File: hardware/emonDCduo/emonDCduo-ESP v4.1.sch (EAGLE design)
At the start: 119 parts, among them IC1 ACS750LCA-050, IC2 ACS750LCA-050, Y1 32Khz

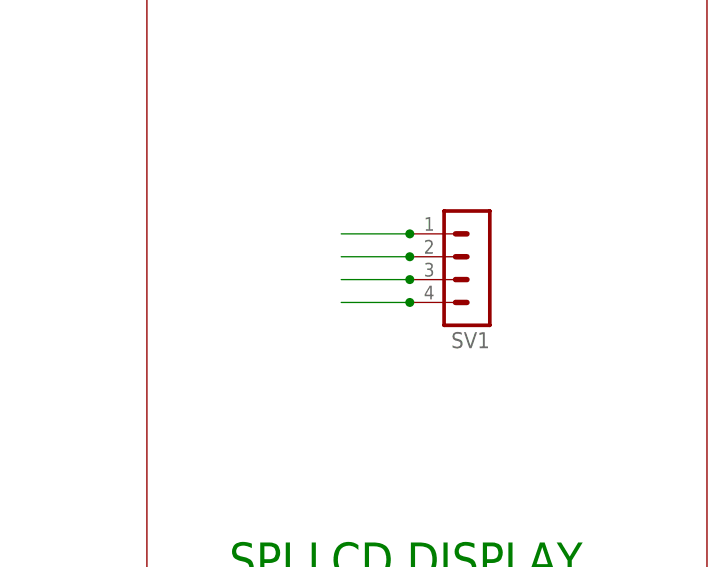
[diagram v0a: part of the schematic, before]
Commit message: commit v4.1
HV isolation improvements
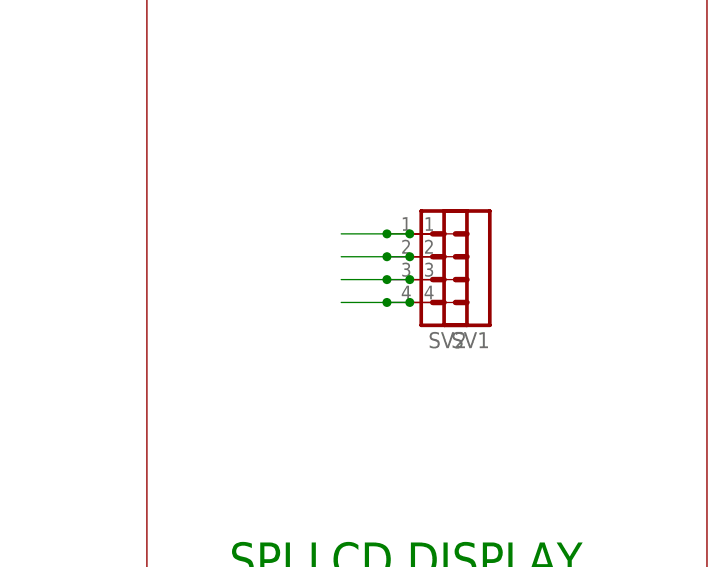
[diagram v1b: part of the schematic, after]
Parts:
- added SV2: (no value), con-lstb:MA04-1
- SJ1, SJ14, SJ3, SJ7: device jumper:SJ -> jumper:SJW
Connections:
- net +3V3: now also SV2.3
- net GND: now also SV2.4
- net SCL: now also SV2.2
- net SDA: now also SV2.1
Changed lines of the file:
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@@
 <?xml version="1.0" encoding="utf-8"?>
 <!DOCTYPE eagle SYSTEM "eagle.dtd">
-<eagle version="9.3.2">
+<eagle version="9.4.0">
 <drawing>
 <settings>
@@
 <clearance class="3" value="0.254"/>
 </class>
+<class number="4" name="HV" width="0" drill="0">
+<clearance class="4" value="0.508"/>
+</class>
 </classes>
 <parts>
@@
 <part name="TP11" library="testpad" library_urn="urn:adsk.eagle:library:385" deviceset="TP" device="PAD1-13Y" package3d_urn="urn:adsk.eagle:package:27947/1"/>
 <part name="D7" library="smf_10" deviceset="SMF*A" device="" technology="6.0"/>
-<part name="SJ3" library="jumper" library_urn="urn:adsk.eagle:library:252" deviceset="SJ" device="" package3d_urn="urn:adsk.eagle:package:15471/1"/>
-<part name="SJ7" library="jumper" library_urn="urn:adsk.eagle:library:252" deviceset="SJ" device="" package3d_urn="urn:adsk.eagle:package:15471/1"/>
+<part name="SJ3" library="jumper" library_urn="urn:adsk.eagle:library:252" deviceset="SJ" device="W" package3d_urn="urn:adsk.eagle:package:15507/1"/>
+<part name="SJ7" library="jumper" library_urn="urn:adsk.eagle:library:252" deviceset="SJ" device="W" package3d_urn="urn:adsk.eagle:package:15507/1"/>
 <part name="SJ8" library="microbuilder" deviceset="SOLDERJUMPER" device="CLOSED"/>
 <part name="SJ9" library="microbuilder" deviceset="SOLDERJUMPER" device="CLOSED"/>
@@
 <attribute name="OC_NEWARK" value=""/>
 </part>
-<part name="SV1" library="con-lstb" library_urn="urn:adsk.eagle:library:162" deviceset="MA04-1" device="" package3d_urn="urn:adsk.eagle:package:8337/1">
+<part name="SV1" library="con-lstb" deviceset="MA04-1" device="" package3d_urn="urn:adsk.eagle:package:8337/1">
 <attribute name="MF" value="MULTICOMP"/>
 <attribute name="MPN" value="2212S-04SG-85"/>
@@
 <part name="U$18" library="testpad_db" deviceset="TP" device="0.8MM"/>
 <part name="U$19" library="testpad_db" deviceset="TP" device="0.8MM"/>
-<part name="SJ1" library="jumper" library_urn="urn:adsk.eagle:library:252" deviceset="SJ" device="" package3d_urn="urn:adsk.eagle:package:15471/1"/>
-<part name="SJ14" library="jumper" library_urn="urn:adsk.eagle:library:252" deviceset="SJ" device="" package3d_urn="urn:adsk.eagle:package:15471/1"/>
+<part name="SJ1" library="jumper" library_urn="urn:adsk.eagle:library:252" deviceset="SJ" device="W" package3d_urn="urn:adsk.eagle:package:15507/1"/>
+<part name="SJ14" library="jumper" library_urn="urn:adsk.eagle:library:252" deviceset="SJ" device="W" package3d_urn="urn:adsk.eagle:package:15507/1"/>
+<part name="SV2" library="con-lstb" deviceset="MA04-1" device="" package3d_urn="urn:adsk.eagle:package:8337/1">
+<attribute name="MF" value="MULTICOMP"/>
+<attribute name="MPN" value="2212S-04SG-85"/>
+<attribute name="OC_FARNELL" value="1593460"/>
+</part>
 </parts>
 <sheets>
@@
 <attribute name="VALUE" x="-97.79" y="363.22" size="1.778" layer="96" rot="R90"/>
 </instance>
+<instance part="SV2" gate="1" x="256.54" y="452.12" smashed="yes" rot="R180">
+<attribute name="VALUE" x="257.81" y="462.28" size="1.778" layer="96" rot="R180"/>
+<attribute name="NAME" x="257.81" y="446.278" size="1.778" layer="95" rot="R180"/>
+</instance>
 </instances>
 <busses>
@@
 <segment>
 <pinref part="SV1" gate="1" pin="4"/>
-<wire x1="251.46" y1="449.58" x2="243.84" y2="449.58" width="0.1524" layer="91"/>
+<wire x1="251.46" y1="449.58" x2="248.92" y2="449.58" width="0.1524" layer="91"/>
 <junction x="251.46" y="449.58"/>
+<pinref part="SV2" gate="1" pin="4"/>
+<wire x1="248.92" y1="449.58" x2="243.84" y2="449.58" width="0.1524" layer="91"/>
+<junction x="248.92" y="449.58"/>
 </segment>
 <segment>
@@
 <segment>
 <pinref part="SV1" gate="1" pin="3"/>
-<wire x1="251.46" y1="452.12" x2="243.84" y2="452.12" width="0.1524" layer="91"/>
+<wire x1="251.46" y1="452.12" x2="248.92" y2="452.12" width="0.1524" layer="91"/>
 <junction x="251.46" y="452.12"/>
+<pinref part="SV2" gate="1" pin="3"/>
+<wire x1="248.92" y1="452.12" x2="243.84" y2="452.12" width="0.1524" layer="91"/>
+<junction x="248.92" y="452.12"/>
 </segment>
 <segment>
@@
 </segment>
 </net>
-<net name="LOAD-NEG-A" class="1">
+<net name="LOAD-NEG-A" class="4">
 <segment>
 <label x="-111.379" y="462.28" size="1.778" layer="95" rot="R180"/>
@@
 </segment>
 </net>
-<net name="SOURCE-POS-B" class="1">
+<net name="SOURCE-POS-B" class="4">
 <segment>
 <pinref part="MH3" gate="G$1" pin="MOUNT"/>
@@
 </segment>
 </net>
-<net name="LOAD-NEG-B" class="1">
+<net name="LOAD-NEG-B" class="4">
 <segment>
 <label x="-111.125" y="354.076" size="1.778" layer="95" rot="R180"/>
@@
 </segment>
 </net>
-<net name="SOURCE-POS-A" class="1">
+<net name="SOURCE-POS-A" class="4">
 <segment>
 <wire x1="-104.14" y1="434.34" x2="-106.68" y2="434.34" width="0.1524" layer="91"/>
@@
 <segment>
 <pinref part="SV1" gate="1" pin="1"/>
-<wire x1="251.46" y1="457.2" x2="243.84" y2="457.2" width="0.1524" layer="91"/>
+<wire x1="251.46" y1="457.2" x2="248.92" y2="457.2" width="0.1524" layer="91"/>
 <junction x="251.46" y="457.2"/>
+<pinref part="SV2" gate="1" pin="1"/>
+<wire x1="248.92" y1="457.2" x2="243.84" y2="457.2" width="0.1524" layer="91"/>
+<junction x="248.92" y="457.2"/>
 </segment>
 <segment>
@@
 <segment>
 <pinref part="SV1" gate="1" pin="2"/>
-<wire x1="251.46" y1="454.66" x2="243.84" y2="454.66" width="0.1524" layer="91"/>
+<wire x1="251.46" y1="454.66" x2="248.92" y2="454.66" width="0.1524" layer="91"/>
 <junction x="251.46" y="454.66"/>
+<pinref part="SV2" gate="1" pin="2"/>
+<wire x1="248.92" y1="454.66" x2="243.84" y2="454.66" width="0.1524" layer="91"/>
+<junction x="248.92" y="454.66"/>
 </segment>
 <segment>
@@
 </segment>
 </net>
-<net name="V_IN_POSTFUSE" class="1">
+<net name="V_IN_POSTFUSE" class="4">
 <segment>
 <wire x1="-111.76" y1="259.08" x2="-109.22" y2="259.08" width="0.1524" layer="91"/>
@@
 </segment>
 </net>
-<net name="V_IN_PREFUSE" class="1">
+<net name="V_IN_PREFUSE" class="4">
 <segment>
 <pinref part="F1" gate="G$1" pin="1"/>

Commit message: commit
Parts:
- SV1, SV2: device con-lstb:MA04-1 -> con-lstb-db:MA04-1
- renumbered REG1 to REG1_5V, REG2 to REG2_3.3
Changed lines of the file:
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@@
 <?xml version="1.0" encoding="utf-8"?>
 <!DOCTYPE eagle SYSTEM "eagle.dtd">
-<eagle version="9.4.0">
+<eagle version="9.3.2">
 <drawing>
 <settings>
@@
 </class>
 <class number="4" name="HV" width="0" drill="0">
-<clearance class="4" value="0.508"/>
+<clearance class="4" value="0.762"/>
 </class>
 </classes>
@@
 <part name="GND2" library="supply1" library_urn="urn:adsk.eagle:library:371" deviceset="GND" device=""/>
 <part name="GND23" library="supply1" library_urn="urn:adsk.eagle:library:371" deviceset="0V" device="" value="GND"/>
-<part name="REG2" library="burr-brown-db" deviceset="REG1117" device="" package3d_urn="urn:adsk.eagle:package:4940/1" value="REG1117-3.3V">
+<part name="REG2_3.3" library="burr-brown-db" deviceset="REG1117" device="" package3d_urn="urn:adsk.eagle:package:4940/1" value="REG1117-3.3V">
 <attribute name="MF" value="TEXAS INSTRUMENTS"/>
 <attribute name="MPN" value="REG1117-3.3"/>
@@
 <part name="J5" library="SparkFun-Connectors" deviceset="CONN_02" device=""/>
 <part name="MICRO_SD" library="MOLEX 47219-2001" deviceset="47219-2001_MICROSD" device=""/>
-<part name="REG1" library="burr-brown-db" deviceset="REG1117" device="" package3d_urn="urn:adsk.eagle:package:4940/1" value="REG1117-5.0V">
+<part name="REG1_5V" library="burr-brown-db" deviceset="REG1117" device="" package3d_urn="urn:adsk.eagle:package:4940/1" value="REG1117-5.0V">
 <attribute name="MF" value="TEXAS INSTRUMENTS"/>
 <attribute name="MPN" value="REG1117-5.0"/>
@@
 <attribute name="OC_NEWARK" value=""/>
 </part>
-<part name="SV1" library="con-lstb" deviceset="MA04-1" device="" package3d_urn="urn:adsk.eagle:package:8337/1">
+<part name="SV1" library="con-lstb-db" deviceset="MA04-1" device="">
 <attribute name="MF" value="MULTICOMP"/>
 <attribute name="MPN" value="2212S-04SG-85"/>
@@
 <part name="SJ1" library="jumper" library_urn="urn:adsk.eagle:library:252" deviceset="SJ" device="W" package3d_urn="urn:adsk.eagle:package:15507/1"/>
 <part name="SJ14" library="jumper" library_urn="urn:adsk.eagle:library:252" deviceset="SJ" device="W" package3d_urn="urn:adsk.eagle:package:15507/1"/>
-<part name="SV2" library="con-lstb" deviceset="MA04-1" device="" package3d_urn="urn:adsk.eagle:package:8337/1">
+<part name="SV2" library="con-lstb-db" deviceset="MA04-1" device="">
 <attribute name="MF" value="MULTICOMP"/>
 <attribute name="MPN" value="2212S-04SG-85"/>
@@
 <attribute name="VALUE" x="145.415" y="220.98" size="1.778" layer="96"/>
 </instance>
-<instance part="REG2" gate="G$1" x="114.3" y="243.84" smashed="yes">
+<instance part="REG2_3.3" gate="G$1" x="114.3" y="243.84" smashed="yes">
 <attribute name="NAME" x="106.68" y="249.555" size="1.778" layer="95" ratio="10"/>
 <attribute name="VALUE" x="106.68" y="251.46" size="1.778" layer="96" ratio="10"/>
@@
 </instance>
 <instance part="MICRO_SD" gate="G$1" x="170.18" y="434.34" smashed="yes"/>
-<instance part="REG1" gate="G$1" x="50.8" y="243.84" smashed="yes">
+<instance part="REG1_5V" gate="G$1" x="50.8" y="243.84" smashed="yes">
 <attribute name="NAME" x="43.18" y="249.555" size="1.778" layer="95" ratio="10"/>
 <attribute name="VALUE" x="43.18" y="251.46" size="1.778" layer="96" ratio="10"/>
@@
 <wire x1="147.32" y1="226.06" x2="129.54" y2="226.06" width="0.1524" layer="91"/>
 <wire x1="129.54" y1="231.14" x2="129.54" y2="226.06" width="0.1524" layer="91"/>
-<pinref part="REG2" gate="G$1" pin="GND"/>
+<pinref part="REG2_3.3" gate="G$1" pin="GND"/>
 <wire x1="114.3" y1="231.14" x2="114.3" y2="226.06" width="0.1524" layer="91"/>
 <wire x1="-101.6" y1="226.06" x2="-101.6" y2="223.52" width="0.1524" layer="91"/>
@@
 <pinref part="GND18" gate="1" pin="0V"/>
 <junction x="-101.6" y="226.06"/>
-<pinref part="REG1" gate="G$1" pin="GND"/>
+<pinref part="REG1_5V" gate="G$1" pin="GND"/>
 <wire x1="50.8" y1="231.14" x2="50.8" y2="226.06" width="0.1524" layer="91"/>
 <junction x="50.8" y="226.06"/>
@@
 <net name="6.5V" class="2">
 <segment>
-<pinref part="REG1" gate="G$1" pin="VIN"/>
+<pinref part="REG1_5V" gate="G$1" pin="VIN"/>
 <wire x1="30.48" y1="243.84" x2="38.1" y2="243.84" width="0.1524" layer="91"/>
 <pinref part="SJ4" gate="1" pin="2"/>
@@
 <wire x1="71.12" y1="238.76" x2="71.12" y2="243.84" width="0.1524" layer="91"/>
 <junction x="71.12" y="243.84"/>
-<pinref part="REG1" gate="G$1" pin="VOUT"/>
+<pinref part="REG1_5V" gate="G$1" pin="VOUT"/>
 <wire x1="63.5" y1="243.84" x2="68.58" y2="243.84" width="0.1524" layer="91"/>
 <wire x1="68.58" y1="243.84" x2="71.12" y2="243.84" width="0.1524" layer="91"/>
@@
 <net name="3.3V_PRE" class="2">
 <segment>
-<pinref part="REG2" gate="G$1" pin="VOUT"/>
+<pinref part="REG2_3.3" gate="G$1" pin="VOUT"/>
 <pinref part="SJ6" gate="1" pin="1"/>
 <wire x1="132.08" y1="243.84" x2="129.54" y2="243.84" width="0.1524" layer="91"/>
@@
 <pinref part="P+3" gate="1" pin="+5V"/>
 <wire x1="91.44" y1="279.4" x2="91.44" y2="274.32" width="0.1524" layer="91"/>
-<pinref part="REG2" gate="G$1" pin="VIN"/>
+<pinref part="REG2_3.3" gate="G$1" pin="VIN"/>
 <wire x1="91.44" y1="274.32" x2="91.44" y2="266.7" width="0.1524" layer="91"/>
 <wire x1="91.44" y1="266.7" x2="91.44" y2="243.84" width="0.1524" layer="91"/>
